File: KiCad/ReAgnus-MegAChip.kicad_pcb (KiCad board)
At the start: 2 copper layers, 78 x 49 mm, 34 parts, among them J2 Conn_02x05_Odd_Even, J3 Conn_02x01, J4 Conn_01x01, J5 Conn_01x01, J6 Conn_01x01, J7 Conn_01x01, U1 PLCC-84-Plug, U10 AS4C4M16SA, U2 LM1117-3.3, U3 SN74CBTD16210, U4 SN74CBTD16210, U5 SN74CBTD16210, U6 SN74CBTD16210, U7 GW1N-UV9LQ144, U8 74LVC1G07, U9 Agnus_TH_plug_pins

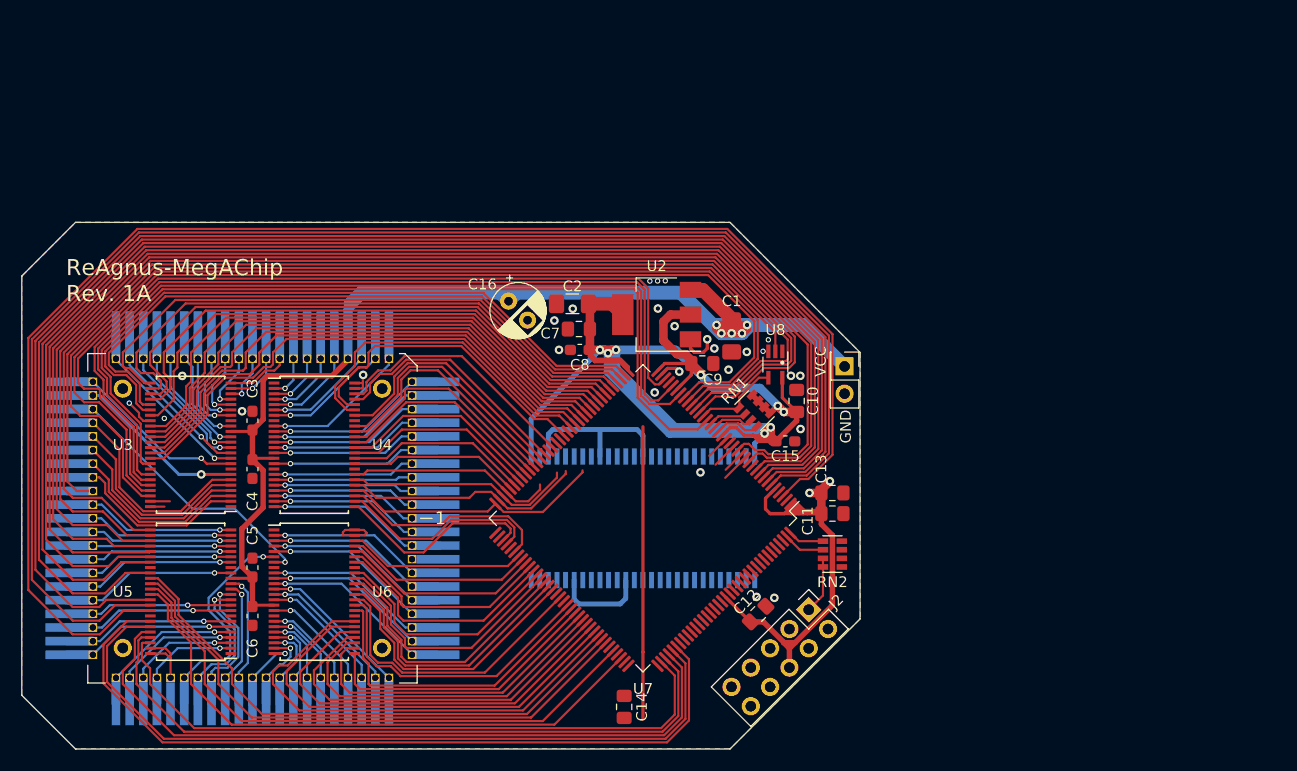
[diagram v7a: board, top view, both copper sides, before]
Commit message: renaming of Capacitors
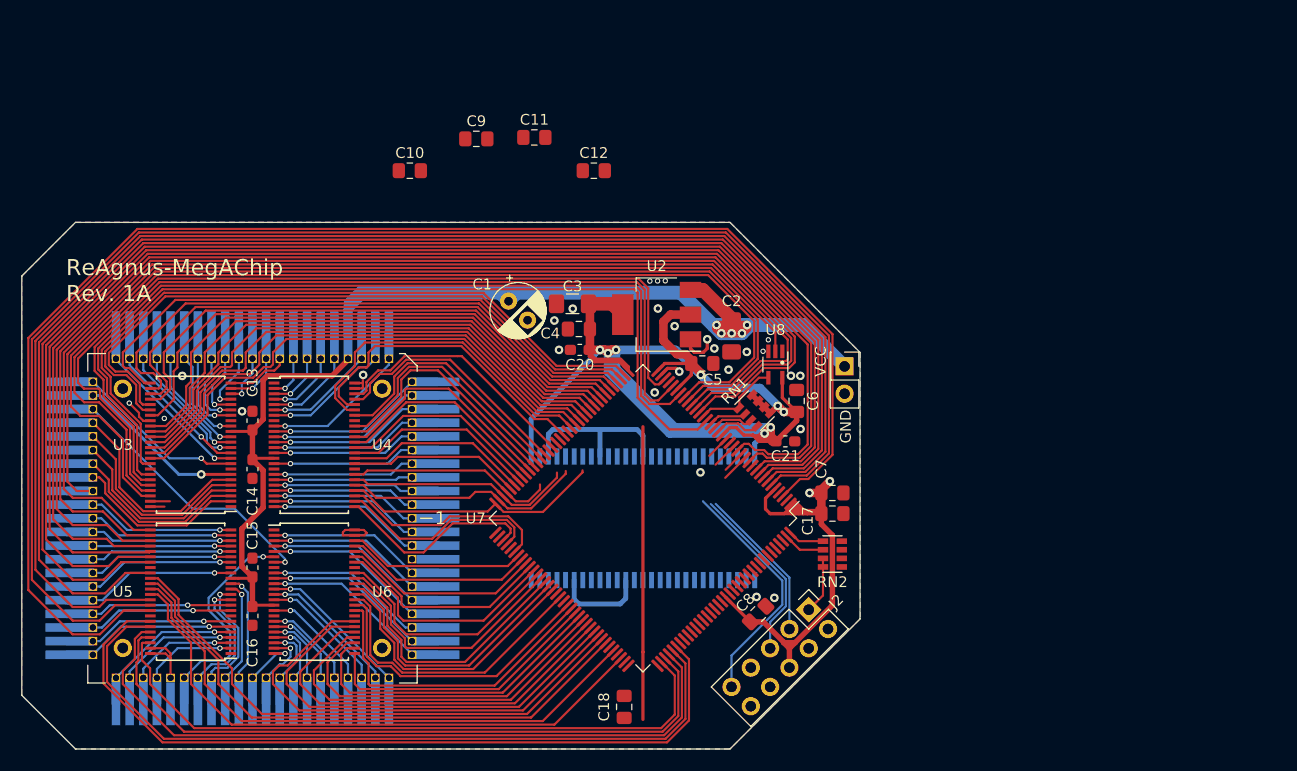
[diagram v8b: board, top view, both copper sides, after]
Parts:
- added C10: 0.1uF, Capacitor_SMD:C_0805_2012Metric_Pad1.15x1.40mm_HandSolder, F.Cu at (153.4, 82.5)
- added C11: 0.1uF, Capacitor_SMD:C_0805_2012Metric_Pad1.15x1.40mm_HandSolder, F.Cu at (165.0, 79.4)
- added C12: 0.1uF, Capacitor_SMD:C_0805_2012Metric_Pad1.15x1.40mm_HandSolder, F.Cu at (170.5, 82.5)
- added C9: 0.1uF, Capacitor_SMD:C_0805_2012Metric_Pad1.15x1.40mm_HandSolder, F.Cu at (159.6, 79.5)
- C1: renamed from C16; value CP_Small -> 100uF Radial Pitch_2.5mm
- C16: renamed from C6; value C_Small -> 0.1uF
- C17: renamed from C11; value 0.1uF -> 0.01uF
- C7: renamed from C13; value 0.01uF -> 0.1uF
- renumbered C3 to C13, C4 to C14, C5 to C15, C14 to C18, C1 to C2, C8 to C20, C15 to C21, C2 to C3, C7 to C4, C9 to C5, C10 to C6, C12 to C8
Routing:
- net TMS: track 2.59 -> 24.9 mm
- net TDO: track 2.19 -> 19.1 mm
- net TDI: track 2.36 -> 16.8 mm
